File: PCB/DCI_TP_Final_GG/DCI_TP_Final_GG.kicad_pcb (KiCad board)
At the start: 2 copper layers, 42 x 90 mm, 69 parts, among them J201 DRIVER A OUT, J301 DRIVER B OUT, J401 IN - Driver A, J402 IN - Driver B, J403 Vin, J404 Vout, U201 A3967, U301 A3967, U401 LM317

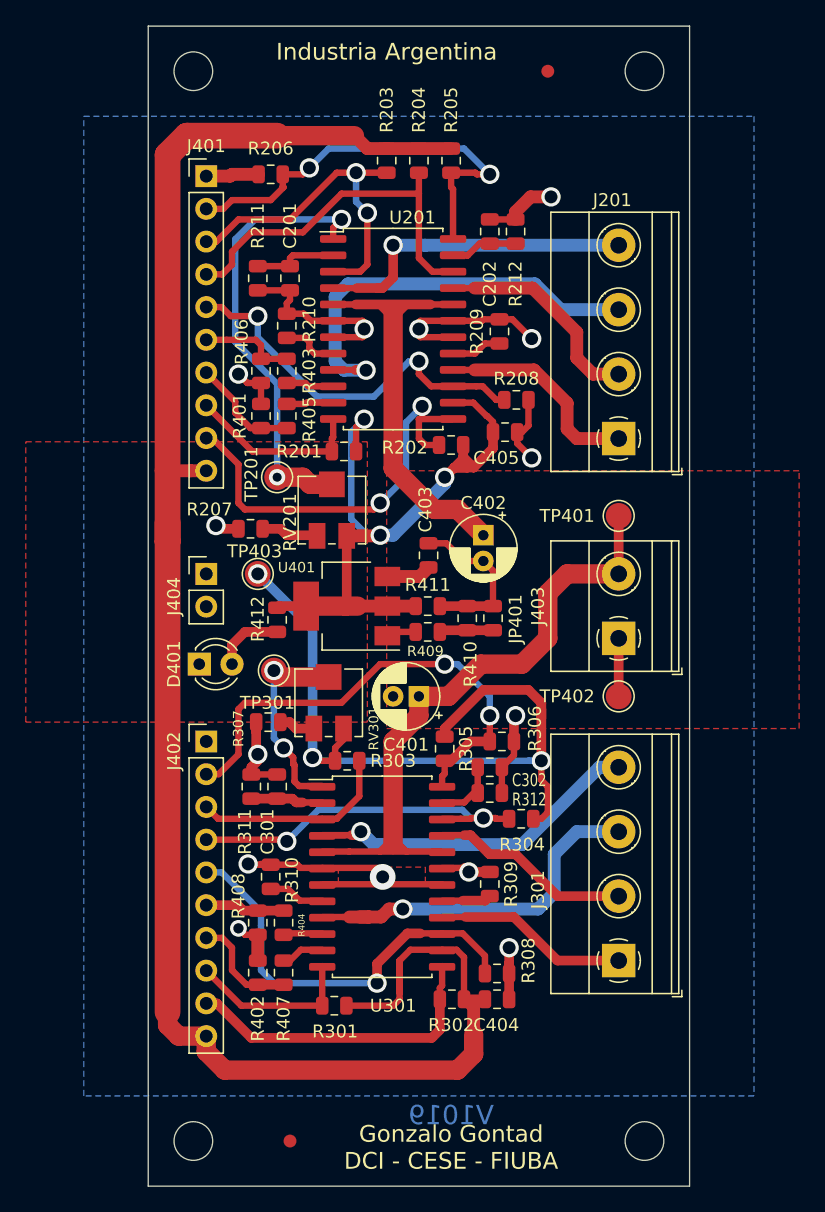
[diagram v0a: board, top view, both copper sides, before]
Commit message: Cambio de ubicacion de capacitores de desacople en la jerarquia del esquematico y actualizacion de identificadores en PCB
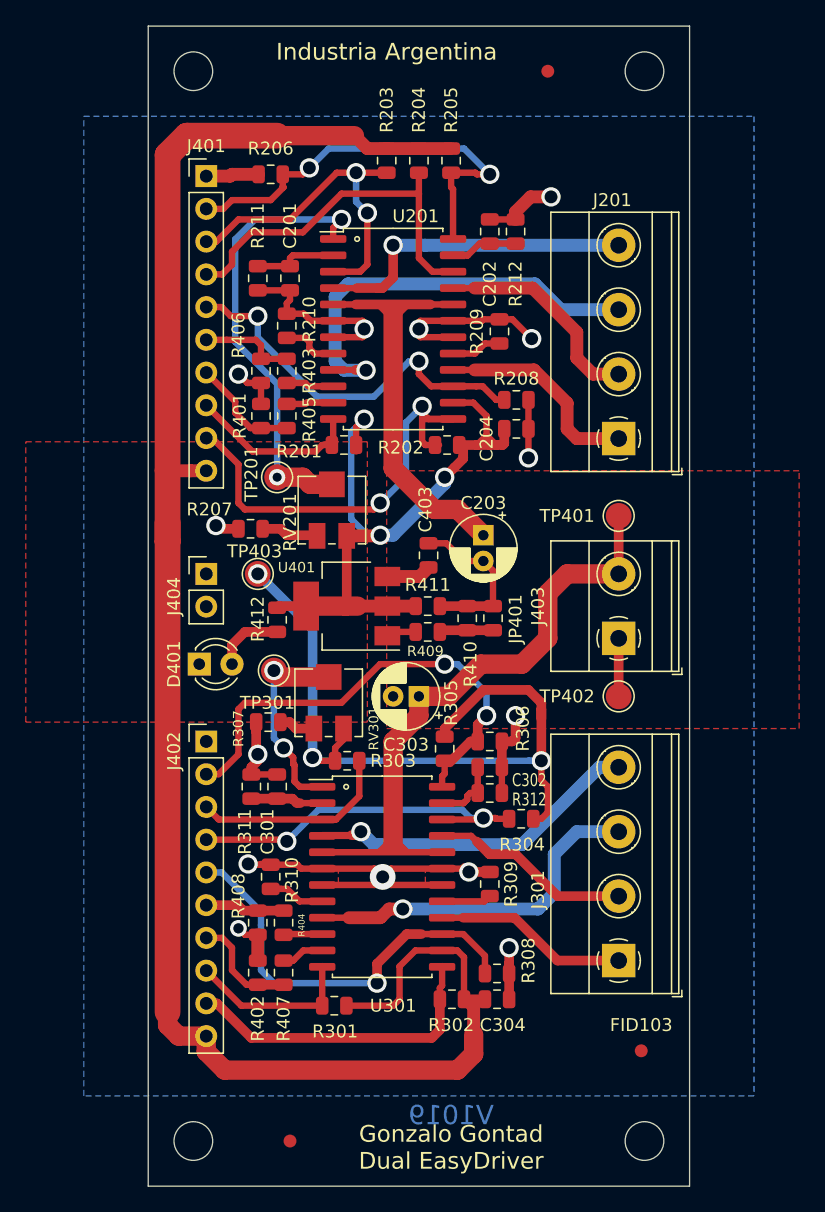
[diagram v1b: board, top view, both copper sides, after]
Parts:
- removed C401, C402: 47uF x 35V, Capacitor_THT:CP_Radial_D5.0mm_P2.00mm
- removed C404, C405: 1uF x 10V, Capacitor_SMD:C_0805_2012Metric
- added C203: 47uF x 35V, Capacitor_THT:CP_Radial_D5.0mm_P2.00mm, F.Cu at (132.5, 90.0)
- added C204: 1uF x 10V, Capacitor_SMD:C_0805_2012Metric, F.Cu at (135.1, 81.8)
- added C303: 47uF x 35V, Capacitor_THT:CP_Radial_D5.0mm_P2.00mm, F.Cu at (127.5, 102.5)
- added C304: 1uF x 10V, Capacitor_SMD:C_0805_2012Metric, F.Cu at (133.6, 126.0)
- added FID103: Fiducial, Fiducial:Fiducial_1mm_Mask2mm, F.Cu at (144.8, 130.0)
- U201, U301: footprint Package_SO:SOIC-24W_7.5x15.4mm_P1.27mm -> DCI_TP_Final_GG:SOIC-24W_7.5x15.4mm_P1.27mm
- moved R306 0.94 mm to (133.0, 106.0)
- moved R201 0.50 mm to (121.7, 83.0)
- moved R202 0.31 mm to (129.7, 83.0)
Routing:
- net GND: track 111.8 -> 117.0 mm
- net VCC: track 268.3 -> 265.6 mm
- net /Driver A/MS2-A: track 33.7 -> 36.3 mm
- net VDD: track 90.0 -> 92.1 mm
- net /Driver B/DB-O2B: track 27.8 -> 29.1 mm
- net Net-(RV301-Pad2): track 17.2 -> 16.1 mm
- net /Driver A/MS1-A: track 13.8 -> 13.0 mm
- net /Driver B/PFD-B: track 38.3 -> 37.5 mm
- net /Driver B/DB-O2A: track 29.0 -> 28.4 mm
- net Net-(C302-Pad1): track 4.75 -> 5.33 mm
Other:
- board text added: "Gonzalo Gontad Dual EasyDriver"
- board text added: "Grilla componentes: 5mm, 2,5mm, 1mm y 0.5mm(para ajuste fino en el control de clearance) Grilla pistas: 1mm, 0.5mm, 0.25mm y 0.1 (para ajuste fino) Vias: 1.3mm ,1.5mm y 2mm (Limite Mayer=1.27) Agujeros: 0.8mm,0.9mm , 1mm , 1.3mm y 3mm (Limite Mayer = 0.7mm) Pistas: 0.5mm, 0.75mm, 1mm, 1.5mm, 2mm (limite Mayer = 0.3mm) Clearance > 0.3 mm (Limite Mayer=0.3mm) PCB Sustrato: FR4 - 1.6mm de espesor Co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"
- board text removed: "Gonzalo Gontad DCI - CESE - FIUBA"
- board text removed: "Grilla componentes: 5mm, 2,5mm, 1mm y 0.5mm(para ajuste fino en el control de clearance) Grilla pistas: 1mm, 0.5mm, 0.25mm y 0.1 (para ajuste fino) Vias: 1.3mm ,1.5mm y 2mm (Limite Mayer=1.27) Pistas: 0.5mm, 0.75mm, 1mm, 1.5mm, 2mm (limite Mayer = 0.3mm) Clearance > 0.3 mm (Limite Mayer=0.3mm) PCB FR4 - sustratos 1.6mm de espesor Cobre 1 Oz Terminacion HASL"

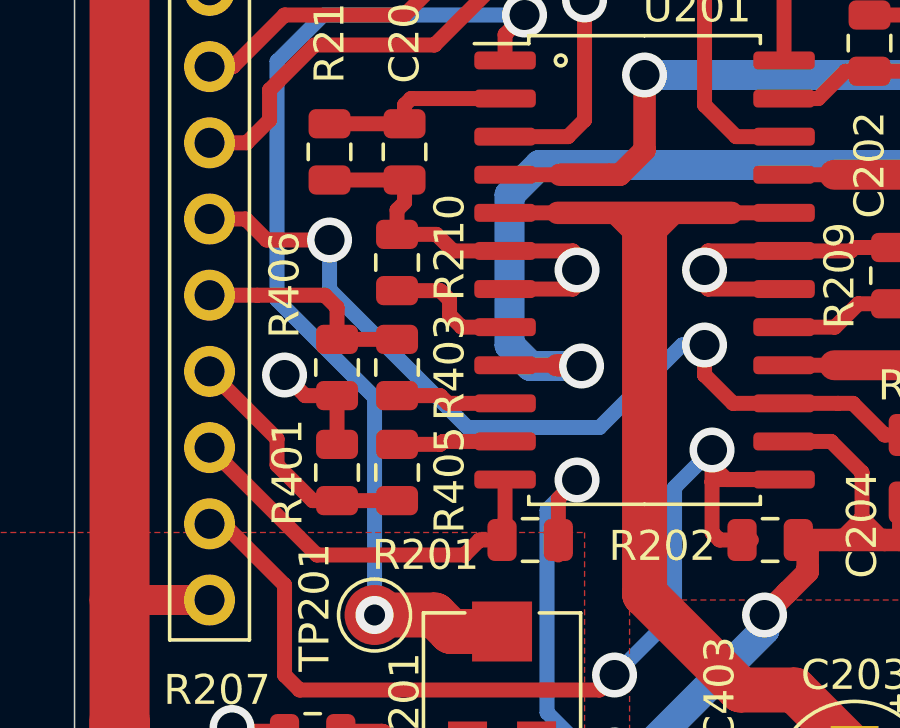
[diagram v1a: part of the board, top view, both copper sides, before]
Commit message: Correccion de Plano de masa
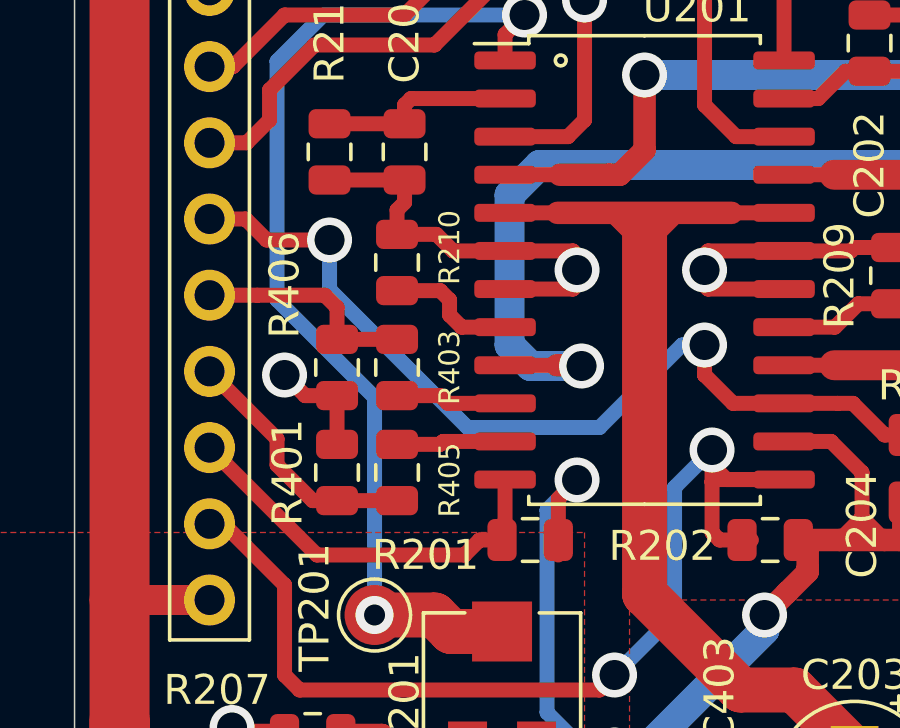
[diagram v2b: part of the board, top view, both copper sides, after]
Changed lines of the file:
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@@
-(kicad_pcb (version 20171130) (host pcbnew 5.1.4-e60b266~84~ubuntu18.04.1)
+(kicad_pcb (version 20171130) (host pcbnew "(5.1.4)-1")
   (general
     (thickness 1.6)
-    (drawings 10)
+    (drawings 11)
     (tracks 568)
     (zones 0)
@@
   (layers
     (0 F.Cu signal hide)
-    (31 B.Cu signal)
+    (31 B.Cu signal hide)
     (32 B.Adhes user hide)
     (33 F.Adhes user hide)
@@
     (45 Margin user hide)
     (46 B.CrtYd user hide)
-    (47 F.CrtYd user)
+    (47 F.CrtYd user hide)
     (48 B.Fab user hide)
     (49 F.Fab user hide)
@@
     (attr smd)
     (fp_text reference R405 (at 0.25 -1.75 90) (layer F.SilkS)
-      (effects (font (size 1 1) (thickness 0.15)))
+      (effects (font (size 0.7 0.7) (thickness 0.15)))
     )
     (fp_text value 1K (at 0 -1.75 90) (layer F.Fab)
@@
     (attr smd)
     (fp_text reference R403 (at 0 -3.75 90) (layer F.SilkS)
-      (effects (font (size 1 1) (thickness 0.15)))
+      (effects (font (size 0.7 0.7) (thickness 0.15)))
     )
     (fp_text value 10K (at 0 1.65 90) (layer F.Fab)
@@
     (attr smd)
     (fp_text reference R210 (at -0.5 -1.75 90) (layer F.SilkS)
-      (effects (font (size 1 1) (thickness 0.15)))
+      (effects (font (size 0.7 0.7) (thickness 0.15)))
     )
     (fp_text value 0.75 (at 0 1.65 90) (layer F.Fab)
@@
     )
   )
+  (gr_text "Grilla componentes: 5mm, 2,5mm,\n 1mm y 0.5mm(para ajuste fino en\nel control de clearance)\n\nGrilla pistas: 1mm, 0.5mm, 0.25mm \ny 0.1 (para ajuste fino)\n\nVias: 1.3mm ,1.5mm y 2mm (Limite Mayer=1.27)\n\nAgujeros: 0.8mm,0.9mm , 1mm , 1.3mm y 3mm\n(Limite Mayer = 0.7mm)\n\nPistas: 0.5mm, 0.75mm, 1mm, 1.5mm, 2mm\n(limite Mayer = 0.3mm)\n\nClearance > 0.3 mm  (Limite Mayer=0.3mm)\n\nPCB\nSustrato: FR4 - 1.6mm de espesor\nCobre: 1 Oz\nTerminación: HASL\n\n" (at 140 87.5) (layer Dwgs.User)
+    (effects (font (size 1 1) (thickness 0.15)) (justify left))
+  )
   (gr_text V1019 (at 130 135) (layer B.Cu)
     (effects (font (size 1.5 1.5) (thickness 0.3)) (justify mirror))
@@
       )
     )
+  )
+  (zone (net 0) (net_name "") (layer B.Cu) (hatch edge 0.508)
+    (connect_pads (clearance 0.508))
+    (min_thickness 0.254)
+    (keepout (tracks allowed) (vias allowed) (copperpour not_allowed))
+    (fill (arc_segments 32) (thermal_gap 0.508) (thermal_bridge_width 0.508))
+    (polygon
+      (pts
+        (xy 122.5 78.5) (xy 120 78.5) (xy 116.5 75) (xy 120 75) (xy 120 77)
+        (xy 121 78) (xy 123 78) (xy 123 78.5)
+      )
+    )
+  )
+  (zone (net 0) (net_name "") (layer B.Cu) (hatch edge 0.508)
+    (connect_pads (clearance 0.508))
+    (min_thickness 0.254)
+    (keepout (tracks allowed) (vias allowed) (copperpour not_allowed))
+    (fill (arc_segments 32) (thermal_gap 0.508) (thermal_bridge_width 0.508))
+    (polygon
+      (pts
+        (xy 125.5 88.5) (xy 128.5 85.5) (xy 129.5 84) (xy 127 84) (xy 127 85.5)
+        (xy 125.5 87)
+      )
+    )
+  )
+  (zone (net 0) (net_name "") (layer B.Cu) (hatch edge 0.508)
+    (connect_pads (clearance 0.508))
+    (min_thickness 0.254)
+    (keepout (tracks allowed) (vias allowed) (copperpour not_allowed))
+    (fill (arc_segments 32) (thermal_gap 0.508) (thermal_bridge_width 0.508))
+    (polygon
+      (pts
+        (xy 123 87.5) (xy 123.5 87.5) (xy 123.5 87) (xy 124 86.5) (xy 124.5 86.5)
+        (xy 126 85) (xy 126 81) (xy 126.5 80.5) (xy 126.5 80) (xy 127 79.5)
+        (xy 127.5 79) (xy 128 79) (xy 128.5 79) (xy 128.5 77) (xy 127.5 77.5)
+        (xy 126.5 77.5) (xy 124 80) (xy 124 80.5) (xy 124 81.5) (xy 123.5 82)
+        (xy 123 82)
+      )
+    )
+  )
+  (zone (net 0) (net_name "") (layer B.Cu) (hatch edge 0.508)
+    (connect_pads (clearance 0.508))
+    (min_thickness 0.254)
+    (keepout (tracks allowed) (vias allowed) (copperpour not_allowed))
+    (fill (arc_segments 32) (thermal_gap 0.508) (thermal_bridge_width 0.508))
+    (polygon
+      (pts
+        (xy 123.5 76) (xy 126.5 76) (xy 125 77.5) (xy 124.5 77.5) (xy 124.5 77)
+      )
+    )
+  )
+  (zone (net 0) (net_name "") (layer B.Cu) (hatch edge 0.508)
+    (connect_pads (clearance 0.508))
+    (min_thickness 0.254)
+    (keepout (tracks allowed) (vias allowed) (copperpour not_allowed))
+    (fill (arc_segments 32) (thermal_gap 0.508) (thermal_bridge_width 0.508))
+    (polygon
+      (pts
+        (xy 119.5 62.5) (xy 119.5 65) (xy 120.5 65) (xy 121 64.5) (xy 122 64.5)
+        (xy 122 63) (xy 122 62.5) (xy 121.5 62) (xy 121.5 61.5) (xy 122 61)
+        (xy 122 60.5) (xy 120.5 60.5) (xy 120 61.5)
+      )
+    )
+  )
+  (zone (net 0) (net_name "") (layer B.Cu) (hatch edge 0.508)
+    (connect_pads (clearance 0.508))
+    (min_thickness 0.254)
+    (keepout (tracks allowed) (vias allowed) (copperpour not_allowed))
+    (fill (arc_segments 32) (thermal_gap 0.508) (thermal_bridge_width 0.508))
+    (polygon
+      (pts
+        (xy 117 80) (xy 121.5 80) (xy 121.5 82) (xy 122 82) (xy 122 81.5)
+        (xy 122.5 80.5) (xy 122.5 79.5) (xy 119.5 79.5) (xy 118 78) (xy 117 78)
+      )
+    )
+  )
+  (zone (net 0) (net_name "") (layer B.Cu) (hatch edge 0.508)
+    (connect_pads (clearance 0.508))
+    (min_thickness 0.254)
+    (keepout (tracks allowed) (vias allowed) (copperpour not_allowed))
+    (fill (arc_segments 32) (thermal_gap 0.508) (thermal_bridge_width 0.508))
+    (polygon
+      (pts
+        (xy 118.5 106) (xy 118 106) (xy 117.5 105.5) (xy 117 105.5) (xy 117 101)
+        (xy 117 100) (xy 116.5 99.5) (xy 118.5 99.5)
+      )
+    )
+  )
+  (zone (net 0) (net_name "") (layer B.Cu) (hatch edge 0.508)
+    (connect_pads (clearance 0.508))
+    (min_thickness 0.254)
+    (keepout (tracks allowed) (vias allowed) (copperpour not_allowed))
+    (fill (arc_segments 32) (thermal_gap 0.508) (thermal_bridge_width 0.508))
+    (polygon
+      (pts
+        (xy 133 113) (xy 133.5 112.5) (xy 133.5 112) (xy 133.5 111.5) (xy 133 111)
+        (xy 137.5 111) (xy 135.5 113)
+      )
+    )
+  )
+  (zone (net 0) (net_name "") (layer B.Cu) (hatch edge 0.508)
+    (connect_pads (clearance 0.508))
+    (min_thickness 0.254)
+    (keepout (tracks allowed) (vias allowed) (copperpour not_allowed))
+    (fill (arc_segments 32) (thermal_gap 0.508) (thermal_bridge_width 0.508))
+    (polygon
+      (pts
+        (xy 122 113) (xy 119 113) (xy 120 112) (xy 122 112) (xy 122.5 112)
+      )
+    )
+  )
+  (zone (net 0) (net_name "") (layer F.Cu) (hatch edge 0.508)
+    (connect_pads (clearance 0.508))
+    (min_thickness 0.254)
+    (keepout (tracks allowed) (vias allowed) (copperpour not_allowed))
+    (fill (arc_segments 32) (thermal_gap 0.508) (thermal_bridge_width 0.508))
+    (polygon
+      (pts
+        (xy 124 99.5) (xy 121.5 99.5) (xy 122 100) (xy 122 101.5)
+      )
+    )
+  )
+  (zone (net 0) (net_name "") (layer F.Cu) (hatch edge 0.508)
+    (connect_pads (clearance 0.508))
+    (min_thickness 0.254)
+    (keepout (tracks allowed) (vias allowed) (copperpour not_allowed))
+    (fill (arc_segments 32) (thermal_gap 0.508) (thermal_bridge_width 0.508))
+    (polygon
+      (pts
+        (xy 129 92) (xy 130.5 92) (xy 129.5 91) (xy 129 91)
+      )
+    )
+  )
+  (zone (net 0) (net_name "") (layer F.Cu) (hatch edge 0.508)
+    (connect_pads (clearance 0.508))
+    (min_thickness 0.254)
+    (keepout (tracks allowed) (vias allowed) (copperpour not_allowed))
+    (fill (arc_segments 32) (thermal_gap 0.508) (thermal_bridge_width 0.508))
+    (polygon
+      (pts
+        (xy 122 87.5) (xy 123.5 87.5) (xy 124 86.5) (xy 124 84) (xy 119 84)
+        (xy 119 84.5) (xy 119.5 85) (xy 122 85)
+      )
+    )
+  )
+  (zone (net 0) (net_name "") (layer B.Cu) (hatch edge 0.508)
+    (connect_pads (clearance 0.508))
+    (min_thickness 0.254)
+    (keepout (tracks allowed) (vias allowed) (copperpour not_allowed))
+    (fill (arc_segments 32) (thermal_gap 0.508) (thermal_bridge_width 0.508))
+    (polygon
+      (pts
+        (xy 140.5 84) (xy 141.5 85) (xy 144.5 85) (xy 145.5 84) (xy 145.5 65.5)
+        (xy 144.5 64.5) (xy 141.5 64.5) (xy 140.5 65.5)
+      )
+    )
+  )
+  (zone (net 0) (net_name "") (layer B.Cu) (hatch edge 0.508)
+    (connect_pads (clearance 0.508))
+    (min_thickness 0.254)
+    (keepout (tracks allowed) (vias allowed) (copperpour not_allowed))
+    (fill (arc_segments 32) (thermal_gap 0.508) (thermal_bridge_width 0.508))
+    (polygon
+      (pts
+        (xy 140.5 125) (xy 141.5 126) (xy 144.5 126) (xy 145.5 125) (xy 145.5 106.5)
+        (xy 144.5 105.5) (xy 141.5 105.5) (xy 140.5 106.5)
+      )
+    )
